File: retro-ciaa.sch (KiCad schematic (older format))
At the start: 113 parts, among them P1 VIDEO OUT, P10 SPI PORT, P11 I²C PORT, P12 ADC PORT, P2 RGBHV TEST POINTS, P3 GAMEPAD 2, P4 P2 PORT, P5 P1 PORT, P6 GAMEPAD 1, P7 WIFI MODULE UART, P8 WIFI MODULE BOOT, P9 AUDIO LINE OUT, U1 VGA SYNC/JOY BUFFER, U2 VGA RGB BUFFER, U3 E-DDC I²C BUFFER, U4 1Mbit EEPROM, U5 I²S AUDIO DAC, U6 WIFI MODULE, U7 BACKLIGHT COVER

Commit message: Esquematico hierarchical sheets A4 terminado, 1.1.1
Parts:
- removed C1, C17: 10uF, Capacitors_SMD:C_1206, symbol C
- removed C10, C11: 100uF, Capacitors_SMD:CP_Elec_6.3x5.8, symbol CP1
- removed C12, C2, C4, C6, C8: 1uF, Capacitors_Tantalum_SMD:CP_Tantalum_Case-A_EIA-3216-18_Reflow, symbol CP1
- removed C13, C16, C22, C24, C26, C28, C3, C30, C5, C7, C9: 100nF, Capacitors_SMD:C_0603, symbol C
- removed C14, C15: 2.2uF, Capacitors_SMD:C_0603, symbol C
- removed C18, C19: 2.2nF, Capacitors_SMD:C_0603, symbol C
- removed C21, C23, C25, C27, C29: 10uF, Capacitors_Tantalum_SMD:CP_Tantalum_Case-A_EIA-3216-18_Reflow, symbol CP1
- removed D1: WHITE BACKLIGHT Y, Salmon:LED_LW_Y1SG, symbol LED_ALT
- removed D2: WHITE BACKLIGHT Z, Salmon:LED_LW_Y1SG, symbol LED_ALT
- removed D3: BAT30, Diodes_SMD:D_SOD-523, symbol D_ALT
- removed G10, G16: RETROCIAA_GAMEPAD, Salmon:RETROCIAA_GAMEPAD, symbol RETROCIAA_GAMEPAD
- removed G11: RETROCIAA_BLUETOOTH, Salmon:RETROCIAA_BLUETOOTH, symbol RETROCIAA_BLUETOOTH
- removed G12: RETROCIAA_AUDIO, Salmon:RETROCIAA_AUDIO, symbol RETROCIAA_AUDIO
- removed G13: RETROCIAA_1, Salmon:RETROCIAA_1, symbol RETROCIAA_1
- removed G14: RETROCIAA_2, Salmon:RETROCIAA_2, symbol RETROCIAA_2
- removed G15: RETROCIAA_VIDEO, Salmon:RETROCIAA_VIDEO, symbol RETROCIAA_VIDEO
- removed G2: RETROCIAA_LOGO, Salmon:RETROCIAA_LOGO, symbol RETROCIAA_LOGO
- removed G3: LOGO BACKLIGHT, Salmon:TREX_LOGO_BACK, symbol INVADER_LOGO_BACK
- removed G4: RETRO-CIAA BACKLIGHT, Salmon:RETROCIAA_LOGO_BACK, symbol RETROCIAA_LOGO_BACK
- removed G5: LOGO_FRONT, Salmon:TREX_LOGO_FRONT, symbol TREX_LOGO_FRONT
- removed G6: RETROCIAA_LOGO_FRONT, Salmon:RETROCIAA_LOGO_FRONT, symbol RETROCIAA_LOGO_FRONT
- removed G7: RETROCIAA_VIDEO_CONN, Salmon:RETROCIAA_VIDEO_CONN, symbol RETROCIAA_VIDEO_CONN
- removed G8: RETROCIAA_LINEOUT, Salmon:RETROCIAA_LINEOUT, symbol RETROCIAA_LINEOUT
- removed G9: RETROCIAA_WIFI, Salmon:RETROCIAA_WIFI, symbol RETROCIAA_WIFI
- removed H1, H2, H3, H4: PCB Hole, Mounting_Holes:MountingHole_3.7mm_Pad_Via, symbol PCB_Hole
- removed LABEL1: ESD_LOGO_15, Salmon:ESD_Sign_12, symbol ESD_LOGO_15
- removed P1: VIDEO OUT, Connectors_DSub:DSUB-15-HD_Female_Horizontal_Pitch2.29x1.98mm_EdgePinOffset8.35mm_Housed_MountingHolesOffset10.89mm, symbol DB15HD_VGA
- removed P10: SPI PORT, Pin_Headers:Pin_Header_Straight_2x04_Pitch2.54mm, symbol CONN_02X04
- removed P11: I²C PORT, Pin_Headers:Pin_Header_Straight_2x04_Pitch2.54mm, symbol CONN_02X04
- removed P12: ADC PORT, Pin_Headers:Pin_Header_Straight_2x04_Pitch2.54mm, symbol CONN_02X04
- removed P2: RGBHV TEST POINTS, Pin_Headers:Pin_Header_Straight_1x06_Pitch2.54mm, symbol CONN_01X06
- removed P3: GAMEPAD 2, Connectors_DSub:DSUB-9_Male_Horizontal_Pitch2.77x2.84mm_EdgePinOffset7.70mm_Housed_MountingHolesOffset9.12mm, symbol DB9S_NES8
- removed P4: P2 PORT, Salmon:Pin_Header_Back_2x20_Pitch2.54mm, symbol EDU-CIAA_P2_2
- removed P5: P1 PORT, Salmon:Pin_Header_Back_2x20_Pitch2.54mm, symbol EDU-CIAA_P1_2
- removed P6: GAMEPAD 1, Connectors_DSub:DSUB-9_Male_Horizontal_Pitch2.77x2.84mm_EdgePinOffset7.70mm_Housed_MountingHolesOffset9.12mm, symbol DB9S_NES8
- removed P7: WIFI MODULE UART, Pin_Headers:Pin_Header_Straight_2x04_Pitch2.54mm, symbol CONN_02X04
- removed P8: WIFI MODULE BOOT, Pin_Headers:Pin_Header_Straight_1x02_Pitch2.54mm, symbol CONN_01X02
- removed P9: AUDIO LINE OUT, Salmon:CUI_SJ-2509N, symbol AudioJack2.5mm
- removed R1, R19, R2, R20, R21, R22, R23, R24, R25, R26, R27, R28, R29, R3, R30, R34, R35, R4: 47K, Resistors_SMD:R_0603, symbol R
- removed R10, R32, R33, R7: 2K, Resistors_SMD:R_0603, symbol R
- removed R11, R5, R8: 499, Resistors_SMD:R_0603, symbol R
- removed R12, R6, R9: 1K, Resistors_SMD:R_0603, symbol R
- removed R13, R15, R16, R17, R18, R31: 100, Resistors_SMD:R_0603, symbol R
- removed R14: 0, Resistors_SMD:R_0603, symbol R
- removed R36, R40: 10K, Resistors_SMD:R_0603, symbol R
- removed R37, R39: 470, Resistors_SMD:R_0603, symbol R
- removed R38: 5K9, Resistors_SMD:R_0603, symbol R
- removed U1: VGA SYNC/JOY BUFFER, Housings_SSOP:TSSOP-20_4.4x6.5mm_Pitch0.65mm, symbol SN74ALVC245-RESCUE-retro-ciaa
- removed U2: VGA RGB BUFFER, Housings_SSOP:TSSOP-20_4.4x6.5mm_Pitch0.65mm, symbol SN74ALVC245-RESCUE-retro-ciaa
- removed U3: E-DDC I²C BUFFER, Housings_SSOP:VSSOP-8_3.0x3.0mm_Pitch0.65mm, symbol TCA9617B
- removed U4: 1Mbit EEPROM, Housings_SSOP:TSSOP-8_4.4x3mm_Pitch0.65mm, symbol M24M01-R
- removed U5: I²S AUDIO DAC, Housings_SSOP:TSSOP-20_4.4x6.5mm_Pitch0.65mm, symbol PCM5100A-RESCUE-retro-ciaa
- removed U6: WIFI MODULE, Salmon:ESP-WROOM-32, symbol ESP-WROOM-32-RESCUE-retro-ciaa
- removed U7: BACKLIGHT COVER, Salmon:TE_SHIELD_2118731-2, symbol TE_SHIELD_2118731-2
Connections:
- net labels removed: +3.3V, +3.3VA, +5V, 3V3, 3V3A, 5V, ADC01, ADC02, ADC03, AUDIO_3V3A, AUDIO_CPVDD, AUDIO_DVDD, AUDIO_LDOO, AUDIO_OUTL, AUDIO_OUTR, AUDIO_XSMT, B0, B1, BLUE, DAC, EDDC_5V, EDDC_EN, EDDC_SCL, EDDC_SDA, EDDC_VCC, EEPROM_VCC, G0, G1, G2, GNDA, GREEN, HSYNC, HSYNC_OUT, I2C_VCC, I2S1_TX_SCK, I2S1_TX_SDA, I2S1_TX_WS, JOY1_DATA, JOY1_DATA_IN, JOY2_DATA, JOY2_DATA_IN, JOY_CLK, JOY_CLK_OUT, JOY_LATCH, JOY_LATCH_OUT, LED_Y, LED_Y_OUT, LED_Z, LED_Z_OUT, R0, R1, R2, RED, RGB_VCC, SPI_MISO, SPI_MOSI, SPI_SCK, SYNC_JOY_VCC, VSYNC, VSYNC_OUT, WM_3V3, WM_AT_CTS, WM_AT_RTS, WM_AT_RXD, WM_AT_TXD, WM_BOOT_OPT, WM_DEBUG_RX, WM_DEBUG_TX, WM_EN, ~AUDIO_MUTE, ~RGB_OE, ~SPI_CS1, ~SPI_CS2, ~SPI_CS3, ~SYNC_JOY_OE
- wire segments 317 -> 40
- no-connect marks 38 -> 0
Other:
- note removed: "(A to B)"
- note removed: "+1.8V"
- note removed: "0110000"
- note removed: "1010000"
- note removed: "3-Wire I²S audio source"
- note removed: "3V3 to 5V I²C level translation."
- note removed: "44.1 Khz De-emphasis disabled"
- note removed: "Bridge for "Firmware download"\nLeave open for "SPI Boot""
- note removed: "DEBUG TX/RX: Bootup sequence\nmessages & firmware download"
- note removed: "DEMP"
- note removed: "FLT"
- note removed: "FMT"
- note removed: "I2S Audio data format"
- note removed: "LED supply voltage: 4.83 V\nvoltage drop: 3.3 V Typ.\ncurrent @ 100 Ohm: 15 mA"
- note removed: "LSB"
- note removed: "Line Out impedance: 470 Ohm.\nTypical Line In impedance\n(load): 1K to 10K Ohm."
- note removed: "Low"
- note removed: "MCLK from internal PLL"
- note removed: "MSB"
- note removed: "NES 8 Bit (Family Game) Gamepads\nusing CMOS 4021 shift register."
- note removed: "Normal filter latency"
- note removed: "Output: RGB 3:3:2 0-0.7V p/p\n@ 75 Ohm Impedance."
- note removed: "P1 & P2 ports are the I/O interface\nto -and power supply from- the \nEDU-CIAA-NXP board"
- note removed: "Place close to 3V3 & 5V supplies"
- note removed: "R/W 101011X"
- note removed: "Read"
- note removed: "Required RC\ndelay circuit"
- note removed: "SCK"
- note removed: "Typical "5V" voltage after\nPMEG3020EH schottky: 4.83 V.\nDivider output: 3.038 V."
- note removed: "Weak Pullups to ensure high\nimpedance state during power up."
- note removed: "Write SegIdx"
- moved on the sheet: C20, R41

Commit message: Cambios menores
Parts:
- removed C20: 1nF, Capacitors_SMD:C_1206, symbol C
- removed R41: 1M, Resistors_SMD:R_0805, symbol R

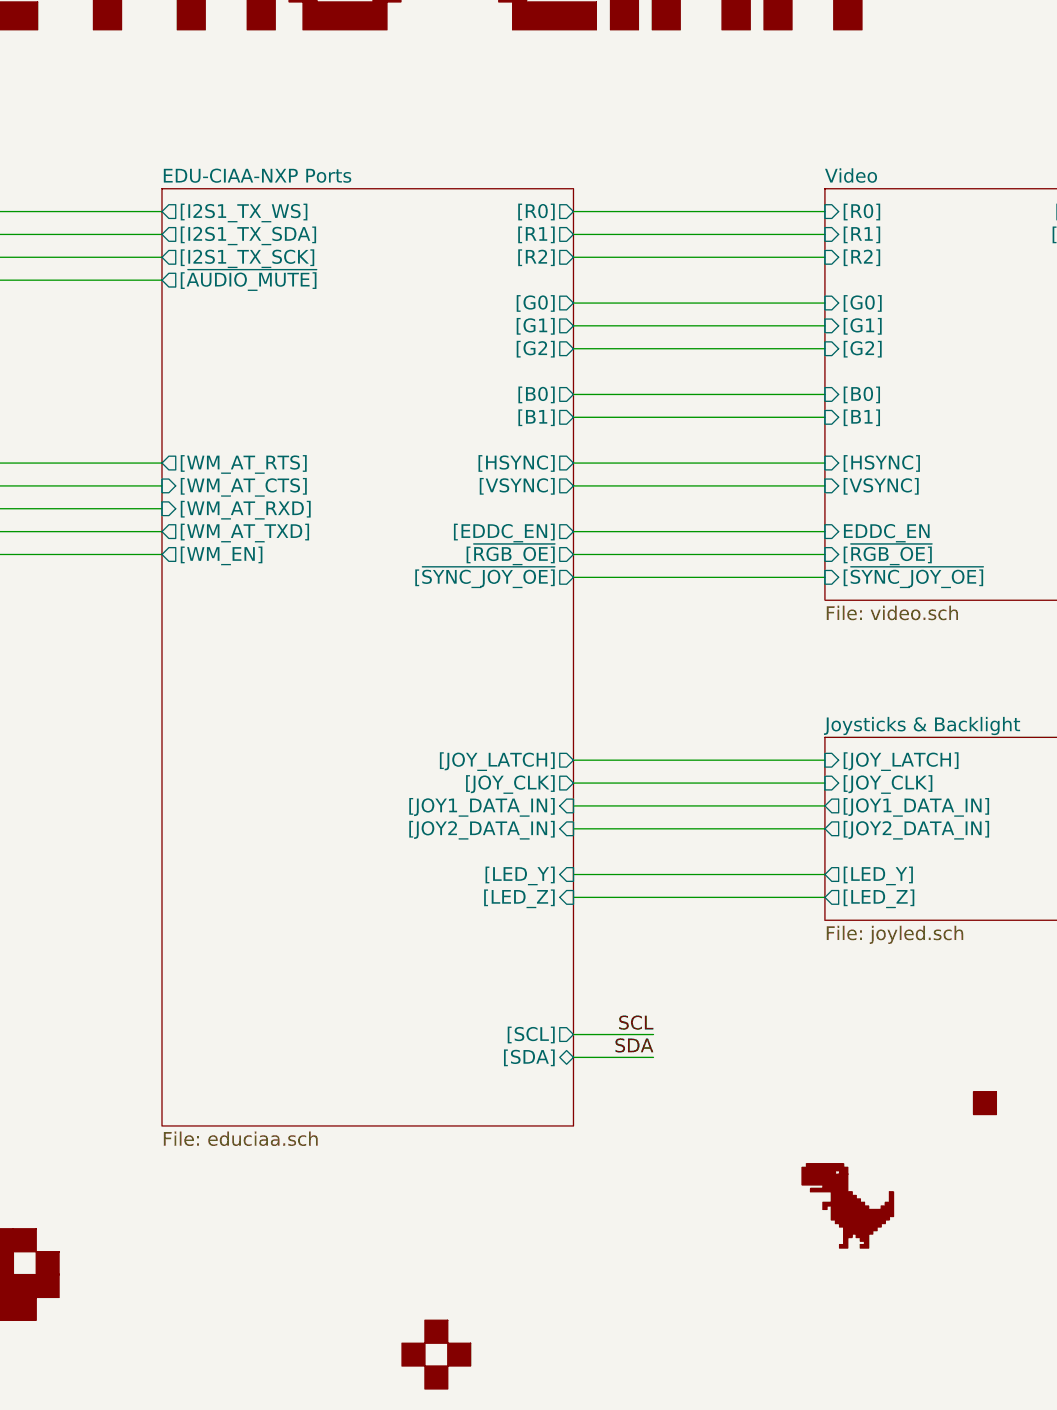
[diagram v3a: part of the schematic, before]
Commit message: Nuevo layout, mejoras y modificaciones del revisor
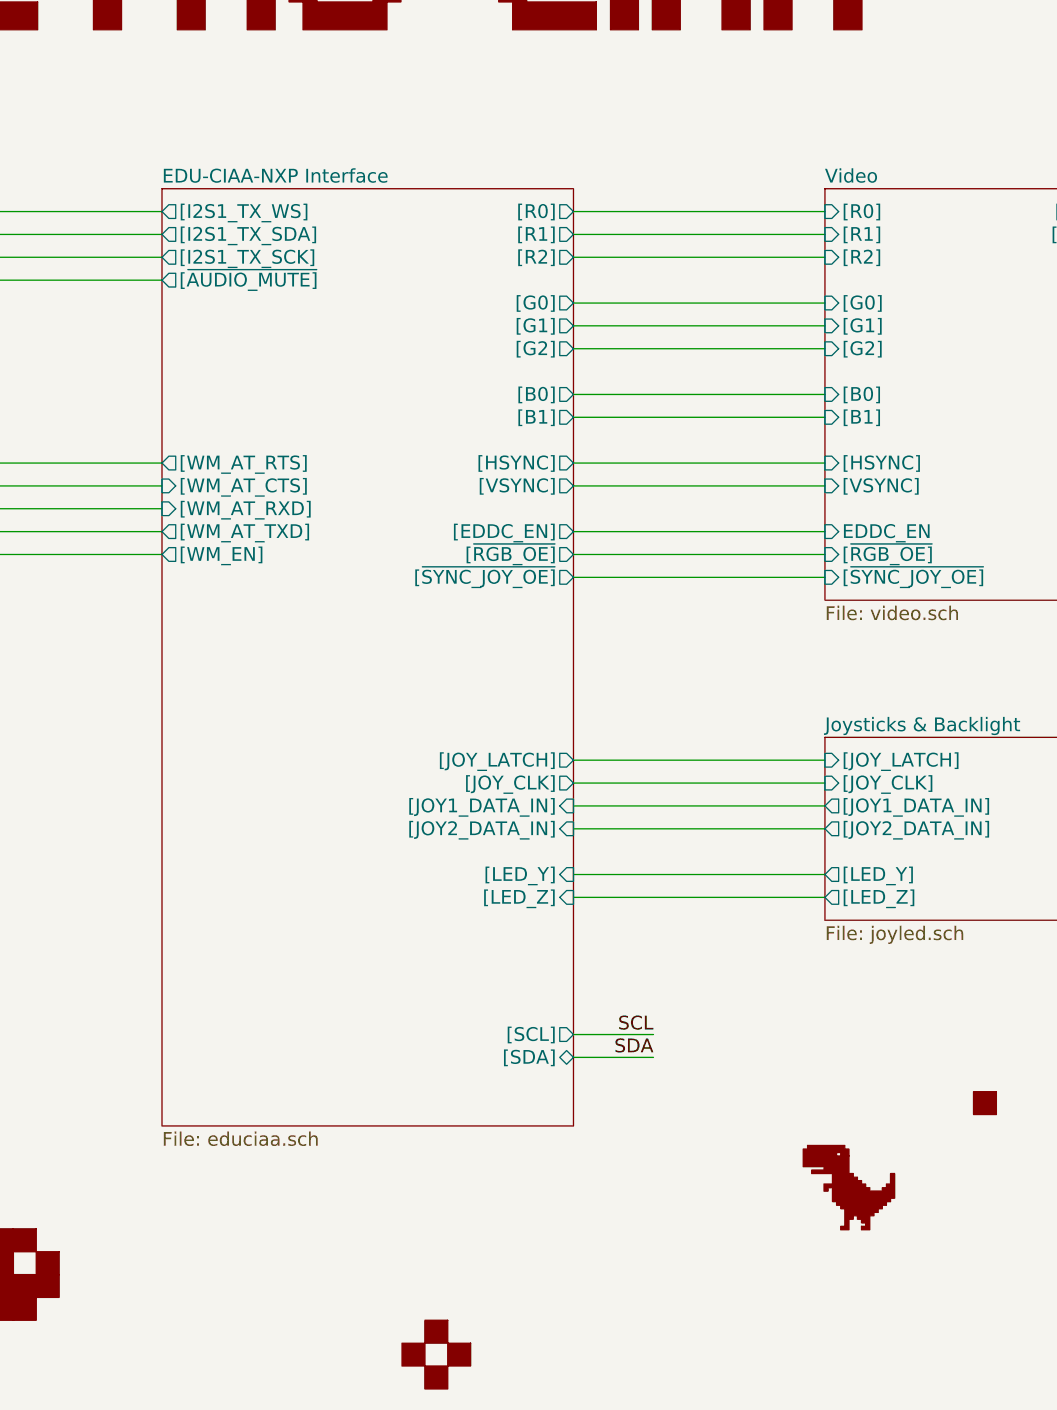
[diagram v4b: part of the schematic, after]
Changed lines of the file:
@@
 EESchema Schematic File Version 2
-LIBS:retro-ciaa-rescue
 LIBS:power
 LIBS:device
@@
 LIBS:contrib
 LIBS:valves
-LIBS:salmon
+LIBS:retro-ciaa
 LIBS:retro-ciaa-cache
 EELAYER 25 0
@@
 encoding utf-8
 Sheet 1 8
-Title "RETRO-CIAA"
-Date "2018-10-19"
+Title "SUBSYSTEMS VIEW"
+Date "2018-10-20"
 Rev "1.1.1"
-Comp "Salmon Robotics"
+Comp "http://www.retro-ciaa.com"
 Comment1 "All resistors 1% & 0603\" unless otherwise noted"
 Comment2 "ERC check OK on 2018-10-19"
@@
 S 5000 1900 1800 4100
 U 5BD1EC50
-F0 "EDU-CIAA-NXP Ports" 60
+F0 "EDU-CIAA-NXP Interface" 60
 F1 "educiaa.sch" 60
 F2 "[VSYNC]" O R 6800 3200 60
@@
 L TREX_SMALL #G1103
 U 1 1 5BD8996B
-P 8000 6350
-F 0 "#G1103" H 8000 6188 60  0001 C CNN
-F 1 "TREX_SMALL" H 8000 6512 60  0001 C CNN
-F 2 "" H 8000 6350 60  0001 C CNN
-F 3 "" H 8000 6350 60  0001 C CNN
-	1    8000 6350
+P 8005 6270
+F 0 "#G1103" H 8005 6108 60  0001 C CNN
+F 1 "TREX_SMALL" H 8005 6432 60  0001 C CNN
+F 2 "" H 8005 6270 60  0001 C CNN
+F 3 "" H 8005 6270 60  0001 C CNN
+	1    8005 6270
 	-1   0    0    -1
 $EndComp

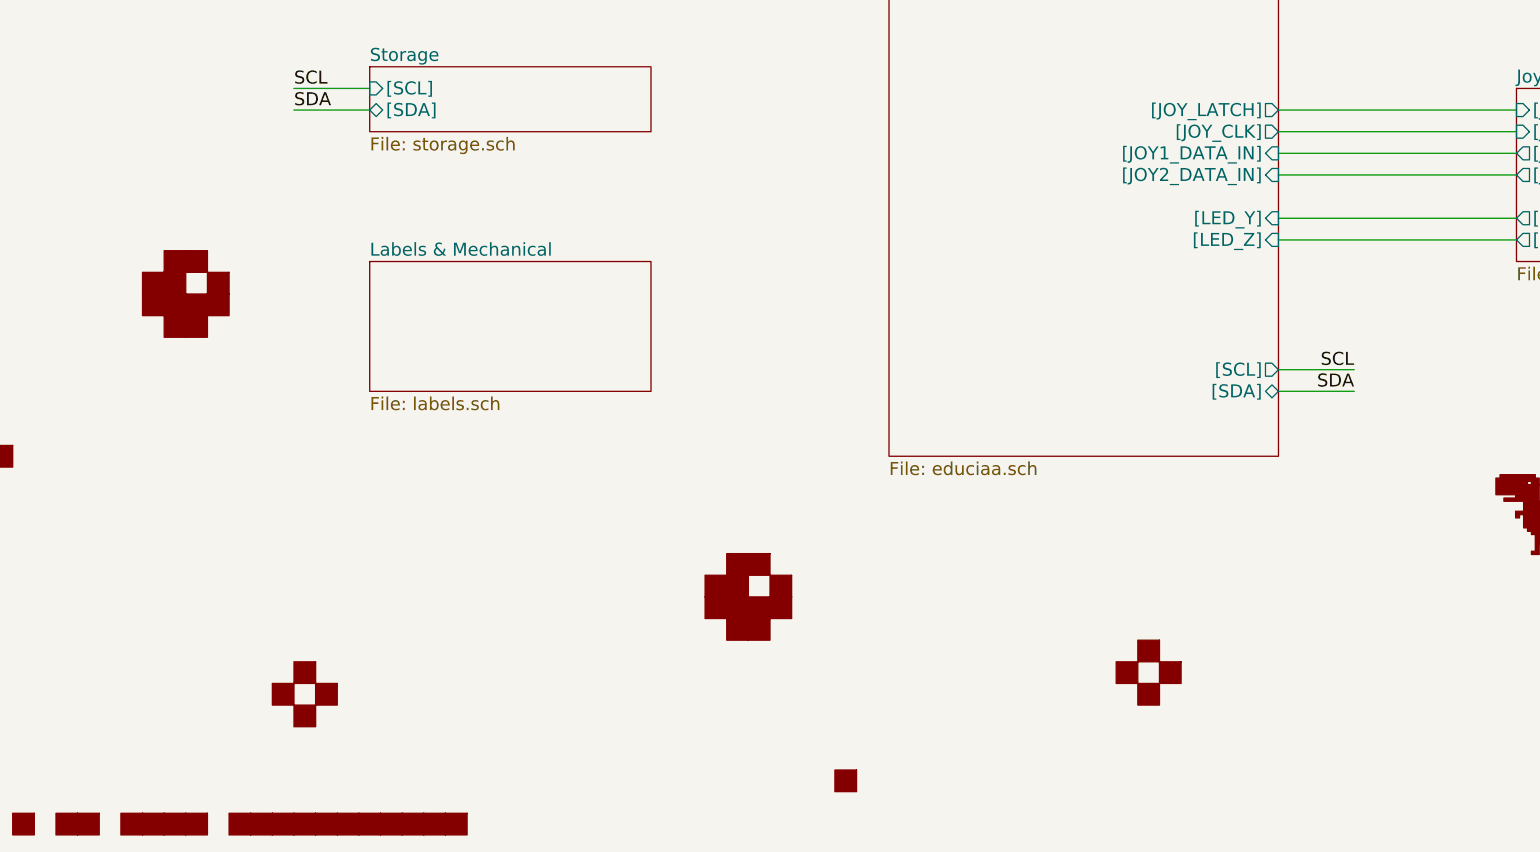
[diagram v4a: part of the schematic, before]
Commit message: Se agrego indice en pagina 1. Union de islas de componentes con cables
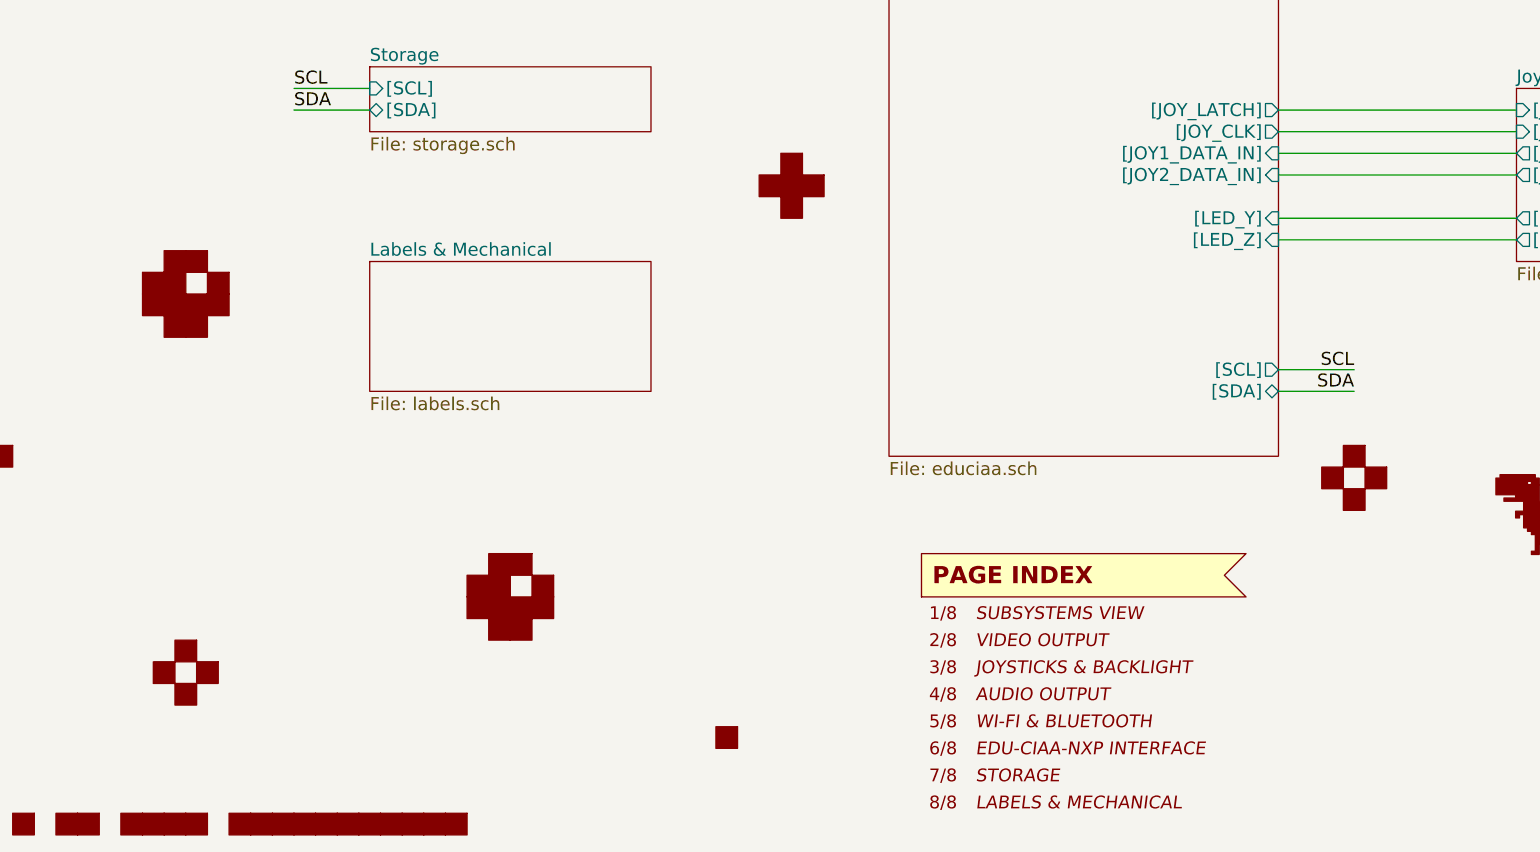
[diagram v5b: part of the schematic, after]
